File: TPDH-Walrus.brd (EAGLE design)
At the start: 16 x 39.9 mm, 44 parts, among them Q2 DMG3404, U1 MS5803-14BA, U2 SN65HVD33RHL, U4 MCP3421A3, U5 TPS79733, U6 MAX6070AAUT18, U7 TXS0102DQM

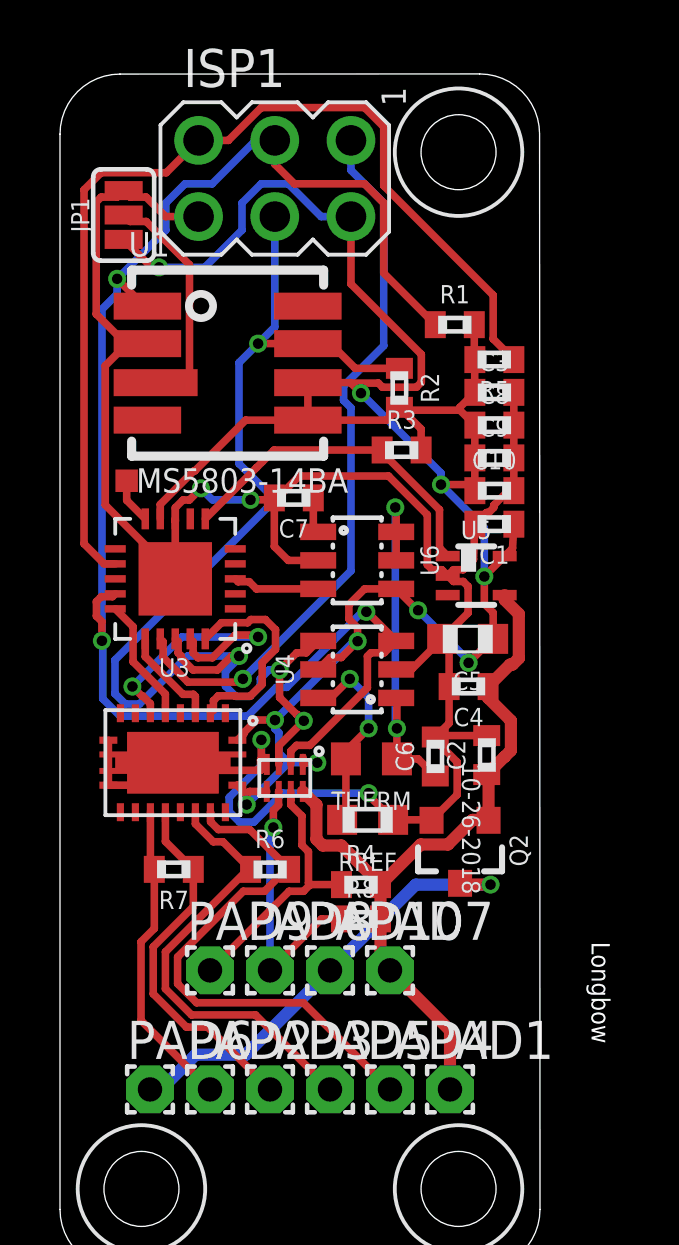
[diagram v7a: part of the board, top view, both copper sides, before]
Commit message: Update +3V3 symbol and re-route
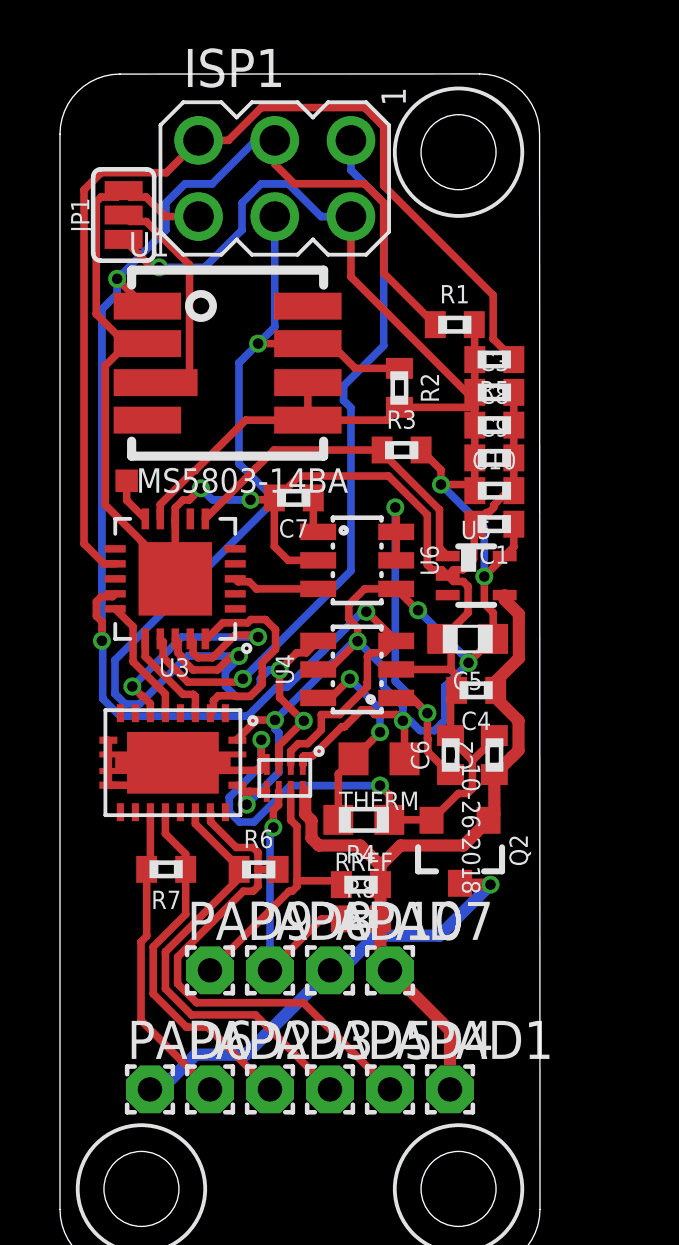
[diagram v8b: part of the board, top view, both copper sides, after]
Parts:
- moved C6 0.51 mm to (13.0, 17.1)
- moved R6 0.38 mm to (6.62, 13.3)
- moved C4 0.28 mm to (13.9, 19.3)
- moved R7 0.25 mm to (3.54, 13.3)
- moved C2 0.25 mm to (14.5, 17.1)
- moved THERM 0.25 mm to (10.6, 17.0)
- moved RREF 0.13 mm to (10.1, 15.0)
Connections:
- removed net 3V3: C1.1, C10.1, C3.1, C5.1, C8.1, C9.1, ISP1.2, JP1.1, R1.2, R2.2, R3.2, R5.2, U1.5, U1.6, U2.1, U2.20, U3.9, U4.5, U5.5, U6.4, U7.1, U7.5
- new net +3V3: C1.1, C10.1, C3.1, C5.1, C8.1, C9.1, ISP1.2, JP1.1, R1.2, R2.2, R3.2, R5.2, THERM.1, U1.5, U1.6, U2.1, U2.20, U3.9, U4.5, U5.5, U6.4, U7.1, U7.5
- net VREF: no longer THERM.1
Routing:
- net +3V3: track 0.00 -> 81.6 mm, vias 0 -> 9
- net 3V3: track 77.7 -> 0.00 mm, vias 10 -> 0
- net GND: track 76.8 -> 77.9 mm
- net RX-: track 14.9 -> 14.4 mm
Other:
- board text removed: "J0"
- board text removed: "Longbow"
